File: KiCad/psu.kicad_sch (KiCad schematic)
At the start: 20 parts, among them J1 Conn_02x04_Top_Bottom, J2 ATX-24, U6 TPS54331

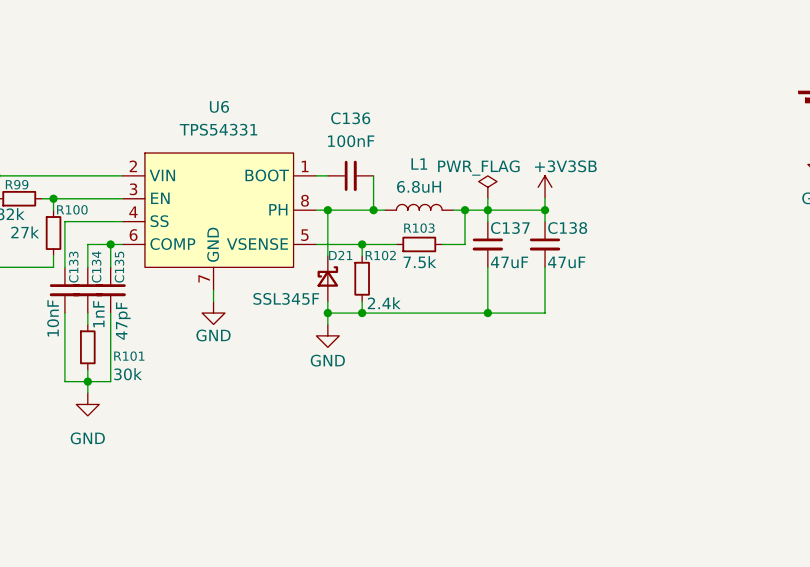
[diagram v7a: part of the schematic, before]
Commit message: Lots of tiny capacitors
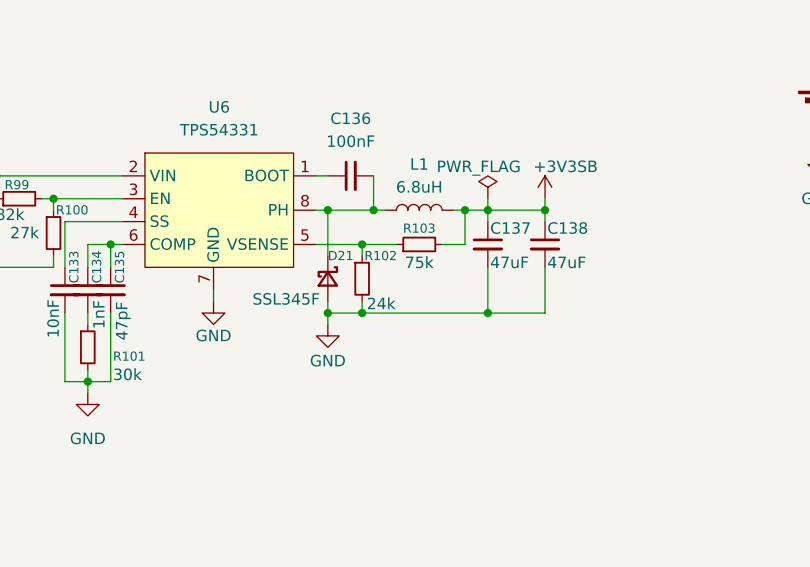
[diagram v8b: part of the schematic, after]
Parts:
- C130, C131, C132, C133, C134, C135, C136: footprint Capacitor_SMD:C_0603_1608Metric -> Capacitor_SMD:C_0402_1005Metric
- R100, R101, R99: footprint (none) -> Resistor_SMD:R_0603_1608Metric
- R102: value 2.4k -> 24k; footprint (none) -> Resistor_SMD:R_0402_1005Metric
- R103: value 7.5k -> 75k; footprint (none) -> Resistor_SMD:R_0402_1005Metric
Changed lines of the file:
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@@
 			)
 		)
-		(property "Footprint" "Capacitor_SMD:C_0603_1608Metric"
+		(property "Footprint" "Capacitor_SMD:C_0402_1005Metric"
 			(at 127 80.01 0)
 			(effects
@@
 			)
 		)
-		(property "Footprint" ""
+		(property "Footprint" "Resistor_SMD:R_0603_1608Metric"
 			(at 93.98 86.36 0)
 			(effects
@@
 			)
 		)
-		(property "Footprint" "Capacitor_SMD:C_0603_1608Metric"
+		(property "Footprint" "Capacitor_SMD:C_0402_1005Metric"
 			(at 95.25 92.71 0)
 			(effects
@@
 			)
 		)
-		(property "Footprint" "Capacitor_SMD:C_0603_1608Metric"
+		(property "Footprint" "Capacitor_SMD:C_0402_1005Metric"
 			(at 100.33 92.71 0)
 			(effects
@@
 			)
 		)
-		(property "Footprint" "Capacitor_SMD:C_0603_1608Metric"
+		(property "Footprint" "Capacitor_SMD:C_0402_1005Metric"
 			(at 78.74 85.09 0)
 			(effects
@@
 			)
 		)
-		(property "Value" "7.5k"
+		(property "Value" "75k"
 			(at 134.62 89.662 90)
 			(effects
@@
 			)
 		)
-		(property "Footprint" ""
+		(property "Footprint" "Resistor_SMD:R_0402_1005Metric"
 			(at 134.62 87.63 0)
 			(effects
@@
 			)
 		)
-		(property "Value" "2.4k"
+		(property "Value" "24k"
 			(at 128.778 94.234 0)
 			(effects
@@
 			)
 		)
-		(property "Footprint" ""
+		(property "Footprint" "Resistor_SMD:R_0402_1005Metric"
 			(at 128.27 91.44 0)
 			(effects
@@
 			)
 		)
-		(property "Footprint" ""
+		(property "Footprint" "Resistor_SMD:R_0603_1608Metric"
 			(at 90.17 82.55 0)
 			(effects
@@
 			)
 		)
-		(property "Footprint" "Capacitor_SMD:C_0603_1608Metric"
+		(property "Footprint" "Capacitor_SMD:C_0402_1005Metric"
 			(at 83.82 85.09 0)
 			(effects
@@
 			)
 		)
-		(property "Footprint" ""
+		(property "Footprint" "Resistor_SMD:R_0603_1608Metric"
 			(at 97.79 99.06 0)
 			(effects
@@
 			)
 		)
-		(property "Footprint" "Capacitor_SMD:C_0603_1608Metric"
+		(property "Footprint" "Capacitor_SMD:C_0402_1005Metric"
 			(at 81.28 85.09 0)
 			(effects
@@
 			)
 		)
-		(property "Footprint" "Capacitor_SMD:C_0603_1608Metric"
+		(property "Footprint" "Capacitor_SMD:C_0402_1005Metric"
 			(at 97.79 92.71 0)
 			(effects
